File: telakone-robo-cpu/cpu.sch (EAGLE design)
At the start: 124 parts, among them K1 629105136821, X1 LIITTIMET_X3815-10, X2 MPT0.5/8-2.54, X3 MPT0.5/8-2.54, X4 MPT0.5/4-2.54, X5 MPT0.5/4-2.54, X7 MPT0.5/4-2.54

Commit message: inputs
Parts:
- removed R35: 5k90 1206, omat_ic_2:RES1206
- added C31, C35: 220u 16V D, EKE:CPOL-EUCT7343
- added C32: 10n, omat_ic_2:CAP0603
- added C33, C34: 2u2 50V 0805, omat_ic_2:CAP0805
- added C36, C37, C49: 100n, omat_ic_2:CAP0603
- added C38: 2u2, omat_ic_2:CAP0603
- added C39: 10n, cpu:CAP0603
- added C40, C41, C42, C43, C44, C45, C46, C48, C50, C51, C52, C56, C57, C59, C60: (no value), cpu:CAP0603
- added D6: LM75BD, omat_ic_2:LM75BD
- added D7: IIS328DQTR, omat_ic_2:IIS328DQTR
- added D8: MAX3430_SA, omat_ic_2:MAX3088_SA
- added D9: 74AHC14, cpu:74AHC14
- added L6: VLP8040-47U, omat_ic_2:VLP8040-47U
- added N2: TPS5430DDA, omat_ic_2:TPS5430DDA
- added Q1, Q2, Q3, Q4: PTC, cpu:PTC
- added R44, R45, R46, R47, R48, R53, R54, R55, R56, R57, R60, R61, R62, R63, R64, R65, R66, R67, R68, R69, R70, R71, R72, R73, R74, R75, R76, R77, R78, R79, R80, R81, R82, R83, R84: (no value), cpu:RES0603
- added R49: 10k0, omat_ic_2:RES0603
- added R50, R85: 5k90, omat_ic_2:RES0603
- added R51, R52, R59: 2k00, omat_ic_2:RES0603
- added R58: 121 1206, omat_ic_2:RES1206
- added V18: SK34A, omat_ic_2:SK34A
- added V19, V20, V21, V22: ESDAXXSC6, cpu:ESDAXXSC6
- added V36: SM712, omat_ic_2:SM712
- C28: value 2u2 -> 100n
- D11: value LM75BD -> 74AHC14; device omat_ic_2:LM75BD -> cpu:74AHC14
- D12: value IIS328DQTR -> 74AHC14; device omat_ic_2:IIS328DQTR -> cpu:74AHC14
- L1: value VLP8040-47U -> SDR1307-15UH; device omat_ic_2:VLP8040-47U -> cpu:INDSDR1307
- R2: value 5k90 -> 3k24
- R28: value 2k00 -> 2k2; device omat_ic_2:RES0603 -> cpu:RES0603
- R29: value 2k00 -> 5k90; device omat_ic_2:RES0603 -> cpu:RES0603
- V13: value SK34A -> SBRD10200; device omat_ic_2:SK34A -> cpu:SBRD10200
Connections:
- net LEDDATA1 renamed DIR1
- net LEDDATA2 renamed DIR3
- net LEDDATA3 renamed DIR5
- net N$3 renamed USBRENUM
- net SERVO10 renamed PULSE4
- net SERVO11 renamed DIR4
- net SERVO12 renamed PULSE5
- net SERVO4 renamed PULSE0
- net SERVO5 renamed DIR0
- net SERVO6 renamed PULSE1
- net SERVO7 renamed PULSE2
- net SERVO8 renamed DIR2
- net SERVO9 renamed PULSE3
- net SERVO_PWM_6 renamed PULSE_1
- removed net N$21: V24.C, V8.C, X3.1
- removed net SERVO_PWM_10: D5.A1
- removed net SERVO_PWM_11: D5.A2
- removed net SERVO_PWM_12: D5.A3
- removed net SERVO_PWM_4: D3.A1
- removed net SERVO_PWM_5: D3.A2
- removed net SERVO_PWM_7: D4.A1
- removed net SERVO_PWM_8: D4.A2
- removed net SERVO_PWM_9: D4.A3
- removed net USART2TX1: D3.A4
- removed net USART2TX2: D4.A4
- removed net USART2TX3: D5.A4
- new net ACCRTXHI: D8.A+, R58.2, V36.1
- new net ACCRTXLO: D8.B-, R58.1, V36.2
- new net DIR_0: D1G$3.PE8, D3.A2
- new net DIR_1: D1G$3.PE9, D3.A4
- new net DIR_2: D1G$3.PE10, D4.A2
- new net DIR_3: D1G$3.PE11, D4.A4
- new net DIR_4: D1G$3.PE12, D5.A2
- new net DIR_5: D1G$3.PE13, D5.A4
- new net ENABLE_N: D1G$3.PE14, D2.OE1, D2.OE2, D2.OE3, D2.OE4, D3.OE1, D3.OE2, D3.OE3, D3.OE4, D4.OE2, D4.OE3, D4.OE4, D5.OE1, D5.OE2, D5.OE3, D5.OE4, R44.1
- new net INPUT0: R29.2, V19.C
- new net INPUT1: R54.2, V19.C1
- new net INPUT10: R74.2, V21.C2
- new net INPUT11: R76.2, V21.C3
- new net INPUT12: R78.2, V22.C
- new net INPUT13: R80.2, V22.C1
- new net INPUT14: R82.2, V22.C2
- new net INPUT15: R84.2, V22.C3
- new net INPUT2: R56.2, V19.C2
- new net INPUT3: R60.2, V19.C3
- new net INPUT4: R62.2, V20.C
- new net INPUT5: R64.2, V20.C1
- new net INPUT6: R66.2, V20.C2
- new net INPUT7: R68.2, V20.C3
- new net INPUT8: R70.2, V21.C
- new net INPUT9: R72.2, V21.C1
- new net INPUT_0: D1G$2.PC8, D9G$1.Y
- new net INPUT_1: D1G$2.PC9, D9G$2.Y
- new net INPUT_10: D11G$5.Y, D1G$2.PD2
- new net INPUT_11: D11G$6.Y, D1G$2.PD3
- new net INPUT_12: D12G$1.Y, D1G$2.PD4
- new net INPUT_13: D12G$2.Y, D1G$2.PD5
- new net INPUT_14: D12G$3.Y, D1G$2.PD6
- new net INPUT_15: D12G$4.Y, D1G$2.PD7
- new net INPUT_2: D1G$2.PC10, D9G$3.Y
- new net INPUT_3: D1G$2.PC11, D9G$4.Y
- new net INPUT_4: D1G$2.PC12, D9G$5.Y
- new net INPUT_5: D1G$2.PC13, D9G$6.Y
- new net INPUT_6: D11G$1.Y, D1G$1.PC14/OSC32IN
- new net INPUT_7: D11G$2.Y, D1G$1.PC15/OSC32OUT
- new net INPUT_8: D11G$3.Y, D1G$2.PD0
- new net INPUT_9: D11G$4.Y, D1G$2.PD1
- new net N$38: C39.1, D9G$1.A, R28.2, R29.1
- new net N$41: C40.1, D9G$2.A, R53.2, R54.1
- new net N$43: C41.1, D9G$3.A, R55.2, R56.1
- new net N$45: C42.1, D9G$4.A, R57.2, R60.1
- new net N$47: C43.1, D9G$5.A, R61.2, R62.1
- new net N$49: C44.1, D9G$6.A, R63.2, R64.1
- new net N$51: C45.1, D11G$1.A, R65.2, R66.1
- new net N$53: C46.1, D11G$2.A, R67.2, R68.1
- new net N$55: C48.1, D11G$3.A, R69.2, R70.1
- new net N$57: C50.1, D11G$4.A, R71.2, R72.1
- new net N$59: C51.1, D11G$5.A, R73.2, R74.1
- new net N$61: C52.1, D11G$6.A, R75.2, R76.1
- new net N$63: C56.1, D12G$1.A, R77.2, R78.1
- new net N$65: C57.1, D12G$2.A, R79.2, R80.1
- new net N$67: C59.1, D12G$3.A, R81.2, R82.1
- new net N$69: C60.1, D12G$4.A, R83.2, R84.1
- new net OUT1X: Q1.1, V24.C, V8.C
- new net OUT2X: Q2.1, V10.C, V24.C1
- new net OUT3X: Q3.1, V11.C, V24.C2
- new net OUT4X: Q4.1, V12.C, V24.C3
- new net OUT_1: D1G$2.PC0, R11.1, V3.G
- new net OUT_2: D1G$2.PC1, R13.1, V5.G
- new net OUT_3: R14.1, V7.G
- new net OUT_4: R15.1, V9.G
- new net PULSE_0: D1G$2.PD12, D3.A1
- new net PULSE_2: D1G$2.PC6, D4.A1
- new net PULSE_3: D1G$3.PE5, D4.A3
- new net PULSE_4: D1G$2.PB8, D5.A1
- new net PULSE_5: D1G$2.PB9, D5.A3
- new net SPI1MISO: D1G$1.PB4/TRSTL
- new net SPI1MOSI: D1G$2.PB5
- new net SPI1SCK: D1G$1.PB3/TDO
- new net SPI_CS_PS2_N: D1G$2.PA8
- new net USART1RX: D1G$2.PA10, D8.RO
- new net USART1TX: D1G$2.PA9, D8.DI
- new net USART1TXE: D1G$2.PD15, D8.DE, D8.RE~, R59.2
- net +12V: now also C33.1, C34.1, N2.VIN, R85.1; no longer R35.1
- net +3V3: now also C31.+, C36.1, C37.1, C38.1, C49.1, D11G$1.VCC, D12G$1.VCC, D6.VCC, D7.CS, D7.RSVD1, D7.VDD, D7.VDDIO, D8.VCC, D9G$1.VCC, L6.B, R44.2, R49.1, R51.2, R52.2; no longer C1.+, D11.VCC, D12.CS, D12.RSVD1, D12.VDD, D12.VDDIO, L1.B, R1.1, R28.2, R29.2
- net +5V: now also C1.+, C35.+, L1.2, R1.1
- net GND: now also C31.-, C33.2, C34.2, C35.-, C36.2, C37.2, C38.2, C39.2, C40.2, C41.2, C42.2, C43.2, C44.2, C45.2, C46.2, C48.2, C49.2, C50.2, C51.2, C52.2, C56.2, C57.2, C59.2, C60.2, D11G$1.GND, D12G$1.GND, D6.A0, D6.A1, D6.A2, D6.GND, D7.EP, D7.GND@1, D7.GND@2, D7.GND@3, D7.GND@4, D7.RSVD2, D7.SAO/SPISDO, D8.GND, D9G$1.GND, N2.EP, N2.GND, R28.1, R45.1, R46.1, R47.1, R48.1, R50.2, R53.1, R55.1, R57.1, R59.1, R61.1, R63.1, R65.1, R67.1, R69.1, R71.1, R73.1, R75.1, R77.1, R79.1, R81.1, R83.1, V18.A, V19.A, V19.A1, V20.A, V20.A1, V21.A, V21.A1, V22.A, V22.A1, V36.3; no longer D11.A0, D11.A1, D11.A2, D11.GND, D12.EP, D12.GND@1, D12.GND@2, D12.GND@3, D12.GND@4, D12.RSVD2, D12.SAO/SPISDO, D2.OE1, D2.OE2, D2.OE3, D2.OE4, D3.OE1, D3.OE2, D3.OE3, D3.OE4, D4.OE2, D4.OE3, D4.OE4, D5.OE1, D5.OE2, D5.OE3, D5.OE4
- net I2C1SCL: now also D6.SCL, D7.SCL/SPICLK, R52.1; no longer D11.SCL, D12.SCL/SPICLK, R29.1
- net I2C1SDA: now also D6.SDA, D7.SDA/SPISDI, R51.1; no longer D11.SDA, D12.SDA/SPISDI, R28.1
- net LEDDATA: now also R48.2
- net MEAS12V: now also R85.2; no longer R35.2
- net N$1: now also L1.1; no longer L1.A
- net N$17: now also C32.1, L6.A, N2.PH, V18.C; no longer V12.C, V24.C3, X3.7
- net N$19: now also C32.2, N2.BOOT; no longer V11.C, V24.C2, X3.5
- net N$20: now also N2.SENSE, R49.2, R50.1; no longer V10.C, V24.C1, X3.3
- net OUT1: now also Q1.2, X3.1; no longer D1G$2.PC0, R11.1, V3.G
- net OUT2: now also Q2.2, X3.3; no longer D1G$2.PC1, R13.1, V5.G
- net OUT3: now also Q3.2, X3.5; no longer R14.1, V7.G
- net OUT4: now also Q4.2, X3.7; no longer R15.1, V9.G
- net SERVO1: now also R45.2
- net SERVO2: now also R46.2
- net SERVO3: now also R47.2
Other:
- note added: "+3.3V 1A"
- note added: "+5V 3A"
- note added: "VMAX 19 V VTH+ 8.1 V VTH- 3.3 V"
- note removed: "I2C1"

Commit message: input liittimet, ena outputit
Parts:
- added C61: 100n, omat_ic_2:CAP0603
- added C62: 2u2, omat_ic_2:CAP0603
- added C63, C64: (no value), cpu:CAP0603
- added C65: (no value), cpu:CAP0805
- added D13, D14: 74AHCT125, cpu:74AHCT125
- added L7: IND0603, omat_ic_2:IND0603
- added L8: IND0603, cpu:IND0603
- added R35, R86, R87, R88, R89, R90, R91, R92, R93, R94, R95, R96: (no value), cpu:RES0603
- added V23, V25: ESDAXXSC6, cpu:ESDAXXSC6
- added X10, X9: MPT0.5/8-2.54, cpu:MPT0.5/8-2.54
- added X11, X12, X13, X14: MPT0.5/4-2.54, cpu:MPT0.5/4-2.54
- added X8: PS-JOYSTICK, cpu:PS-JOYSTICK
- added Y1, Y2, Y3, Y4: PTH2.6-5.5SQ, EKE:PTH2.6-5.5SQ
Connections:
- removed net SPI1SCK: D1G$1.PB3/TDO
- new net ENA0: R89.2, V23.C, X11.1
- new net ENA1: R90.2, V23.C1, X11.2
- new net ENA2: R91.2, V23.C2, X11.3
- new net ENA3: R92.2, V23.C3, X11.4
- new net ENA4: R93.2, V25.C, X12.1
- new net ENA5: R94.2, V25.C1, X12.2
- new net ENA_0: D13.A1, D1G$3.PG0
- new net ENA_1: D13.A2, D1G$3.PG1
- new net ENA_2: D13.A3, D1G$3.PG2
- new net ENA_3: D13.A4, D1G$3.PG3
- new net ENA_4: D14.A1, D1G$3.PG4
- new net ENA_5: D14.A2, D1G$3.PG5
- new net I2CVCC: C65.1, L8.1, X14.1
- new net N$21: R86.1, X8.CMD
- new net N$3: R35.1, X8.DATA
- new net N$39: R87.1, X8.ATT
- new net N$42: R88.1, X8.CLK
- new net N$44: D13.Y1, R89.1
- new net N$46: D13.Y2, R90.1
- new net N$48: D13.Y3, R91.1
- new net N$50: D13.Y4, R92.1
- new net N$52: D14.Y1, R93.1
- new net N$54: D14.Y2, R94.1
- new net N$56: D14.Y3, R95.1
- new net N$58: D14.Y4, R96.1
- new net N$60: X14.2
- new net N$62: X14.4
- new net PSVCC: C61.1, C62.1, L7.1, X8.VCC
- new net SPARE1: R95.2, V25.C2, X12.3
- new net SPARE2: R96.2, V25.C3, X12.4
- new net SPARE_1: D14.A3, D1G$3.PG6
- new net SPARE_2: D14.A4, D1G$3.PG7
- new net SPI1CLK: D1G$1.PB3/TDO, R88.2
- net +12V: now also X13.1, X13.2, X13.3, X13.4
- net +3V3: now also L7.2
- net +5V: now also C63.1, C64.1, D13.VCC, D14.VCC, L8.2
- net ENABLE_N: now also D13.OE1, D13.OE2, D13.OE3, D13.OE4, D14.OE2, D14.OE3, D14.OE4
- net GND: now also C61.2, C62.2, C63.2, C64.2, C65.2, D13.GND, D14.GND, V23.A, V23.A1, V25.A, V25.A1, X14.3, X8.GND, Y1.1, Y2.1, Y3.1, Y4.1
- net INPUT0: now also X9.1
- net INPUT1: now also X9.2
- net INPUT10: now also X10.3
- net INPUT11: now also X10.4
- net INPUT12: now also X10.5
- net INPUT13: now also X10.6
- net INPUT14: now also X10.7
- net INPUT15: now also X10.8
- net INPUT2: now also X9.3
- net INPUT3: now also X9.4
- net INPUT4: now also X9.5
- net INPUT5: now also X9.6
- net INPUT6: now also X9.7
- net INPUT7: now also X9.8
- net INPUT8: now also X10.1
- net INPUT9: now also X10.2
- net SPI1MISO: now also R35.2
- net SPI1MOSI: now also R86.2
- net SPI_CS_PS2_N: now also R87.2
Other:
- note added: "MOUNTING HOLES"
- moved on the sheet: C25, C29, C30, C36, C37, C38, C49, D1G$2, D1G$3, D3, D4, D5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

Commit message: i2c expander yms
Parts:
- added C66, C67: (no value), cpu:CAP0805
- added D15: PCA9517, cpu:PCA9517
- added L9: IND0603, cpu:IND0603
- added R100, R99: 2k00, omat_ic_2:RES0603
- added X15: MPT0.5/4-2.54, cpu:MPT0.5/4-2.54
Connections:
- removed net N$60: X14.2
- removed net N$62: X14.4
- new net I2CSCL: D15.SCLB, R100.1, X14.4
- new net I2CSDA: D15.SDAB, R99.1, X14.2
- net +3V3: now also C67.1, D15.VCCA, L8.2
- net +5V: now also L9.1; no longer L8.2
- net ACCRTXHI: now also X15.3
- net ACCRTXLO: now also X15.4
- net GND: now also C66.2, C67.2, D12G$5.A, D12G$6.A, D15.GND
- net I2C1SCL: now also D15.SCLA
- net I2C1SDA: now also D15.SDAA
- net I2CVCC: now also C66.1, D15.EN, D15.VCCB, L9.2, R100.2, R99.2
- net OUT_3: now also D1G$2.PB10
- net OUT_4: now also D1G$2.PB11
- net SERVO_PWM_3: now also D1G$2.PB0
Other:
- note removed: "TODO SERVO_PWM_3 NOT CONNECTED"
- moved on the sheet: C49, C65, D8, L8, R58, R59, V36

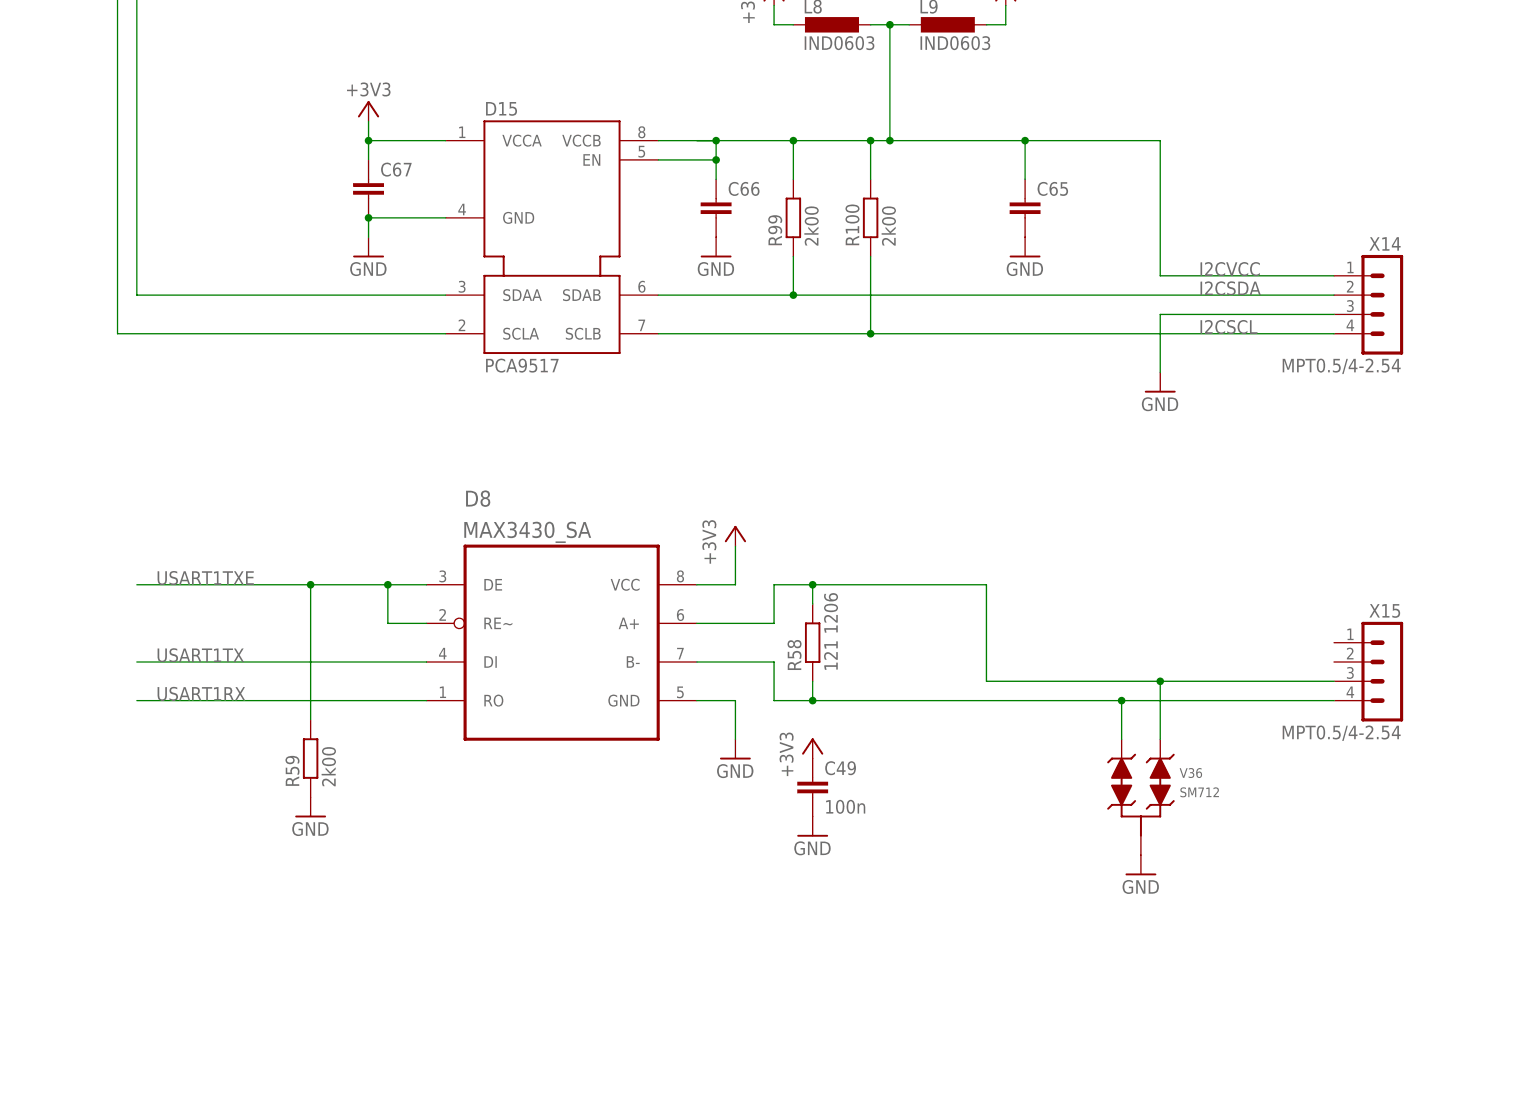
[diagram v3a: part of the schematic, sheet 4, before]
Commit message: finish schematics, rough initial placement
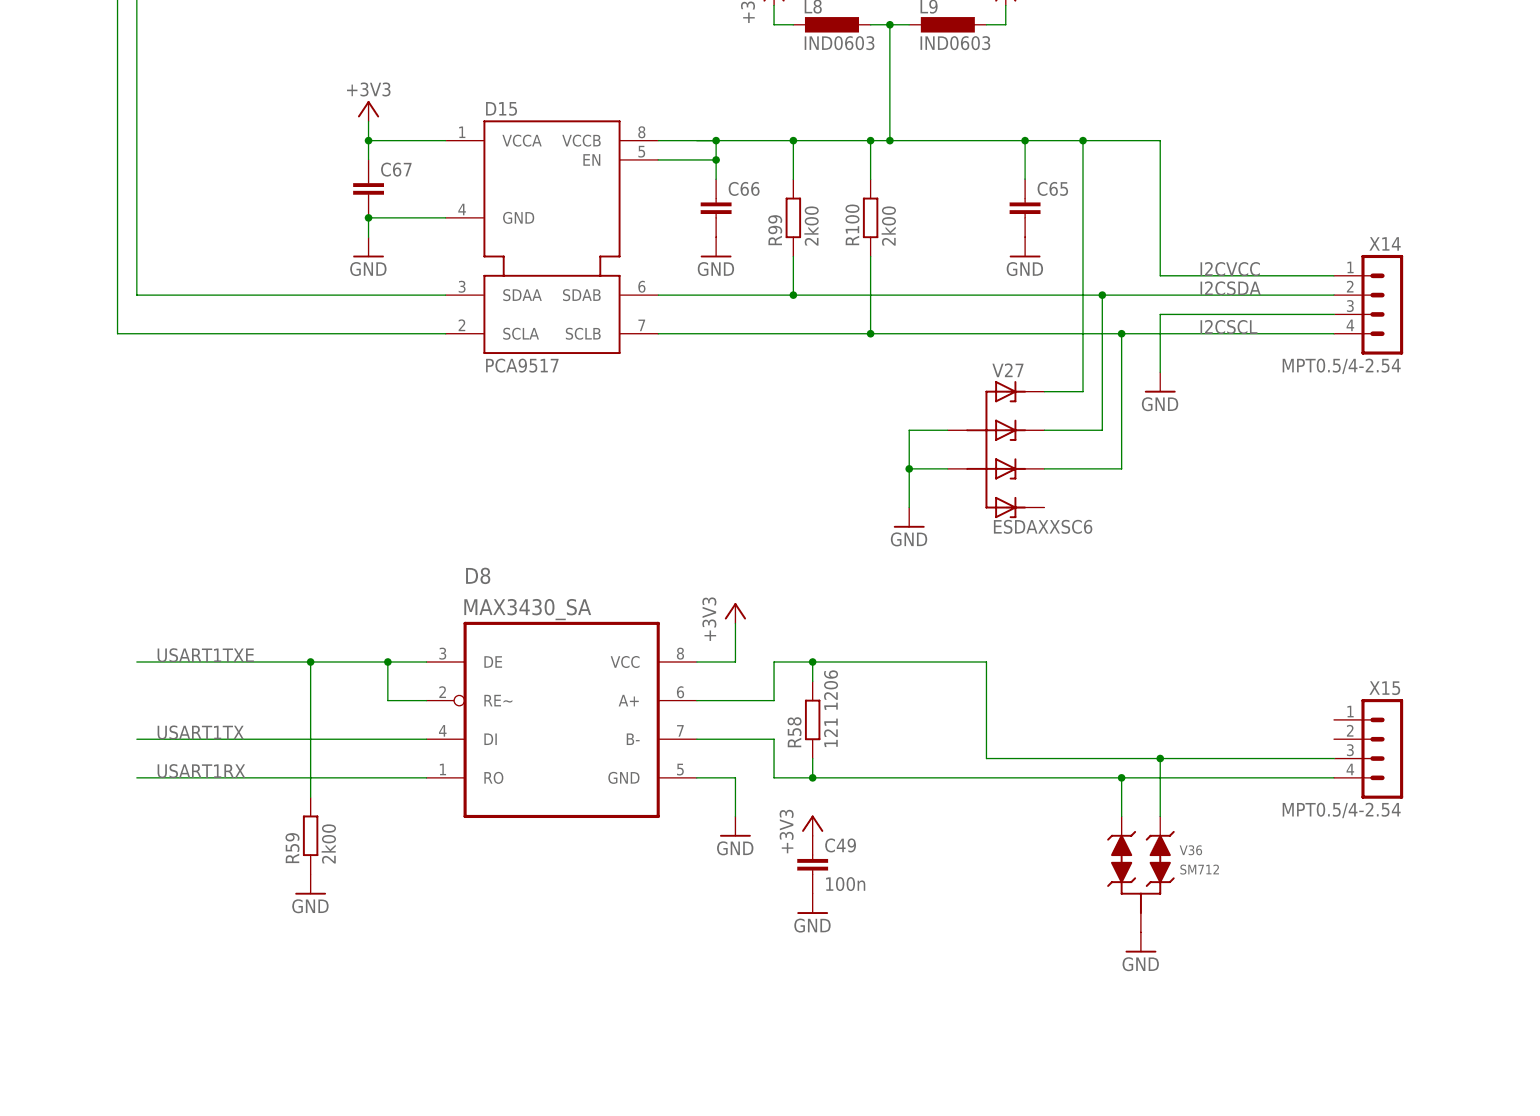
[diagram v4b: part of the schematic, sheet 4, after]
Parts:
- added C68, C69: (no value), cpu:CAP0805
- added V26: SRV05-4, cpu:SRV05-4
- added V27: ESDAXXSC6, cpu:ESDAXXSC6
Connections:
- new net SERVO_VCC1: C68.1
- new net SERVO_VCC2: C69.1
- net GND: now also C68.2, C69.2, V26.GND, V27.A, V27.A1
- net I2CSCL: now also V27.C2
- net I2CSDA: now also V27.C1
- net I2CVCC: now also V27.C
- net USB_DM: now also V26.D
- net USB_DP: now also V26.C
- net VUSB: now also V26.VCC
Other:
- moved on the sheet: C49, C6, C7, D8, L4, L5, R58, R59, V36, X15

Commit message: signals routed, almost
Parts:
- added X16: MPT0.5/4-2.54, cpu:MPT0.5/4-2.54
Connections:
- removed net SERVO_VCC1: C68.1
- removed net SERVO_VCC2: C69.1
- new net ENABLE_PWM_N: D1G$3.PG9, D2.OE1, D2.OE2, D2.OE3, D2.OE4
- net ACCRTXHI: now also V36.2; no longer V36.1
- net ACCRTXLO: now also V36.1; no longer V36.2
- net DIR0: now also V14.C2; no longer V14.C1
- net DIR1: now also V14.C; no longer V14.C3
- net DIR2: now also V15.C2; no longer V15.C1
- net DIR3: now also V15.C; no longer V15.C3
- net DIR4: now also V17.C2; no longer V17.C1
- net DIR5: now also V17.C; no longer V17.C3
- net ENA0: now also V23.C3; no longer V23.C
- net ENA1: now also V23.C2; no longer V23.C1
- net ENA2: now also V23.C1; no longer V23.C2
- net ENA3: now also V23.C; no longer V23.C3
- net ENA4: now also V25.C3; no longer V25.C
- net ENA5: now also V25.C2; no longer V25.C1
- net ENABLE_N: now also D14.OE1, D4.OE1; no longer D2.OE1, D2.OE2, D2.OE3, D2.OE4
- net GND: now also X16.1, X16.4, X2.3, X2.6; no longer X2.5, X2.8
- net I2CSCL: now also V27.C1; no longer V27.C2
- net I2CSDA: now also V27.C2; no longer V27.C1
- net I2CVCC: now also V27.C3; no longer V27.C
- net INPUT0: now also V19.C1; no longer V19.C
- net INPUT1: now also V19.C; no longer V19.C1
- net INPUT10: now also V21.C3; no longer V21.C2
- net INPUT11: now also V21.C2; no longer V21.C3
- net INPUT12: now also V22.C1; no longer V22.C
- net INPUT13: now also V22.C; no longer V22.C1
- net INPUT14: now also V22.C3; no longer V22.C2
- net INPUT15: now also V22.C2; no longer V22.C3
- net INPUT2: now also V19.C3; no longer V19.C2
- net INPUT3: now also V19.C2; no longer V19.C3
- net INPUT4: now also V20.C1; no longer V20.C
- net INPUT5: now also V20.C; no longer V20.C1
- net INPUT6: now also V20.C3; no longer V20.C2
- net INPUT7: now also V20.C2; no longer V20.C3
- net INPUT8: now also V21.C1; no longer V21.C
- net INPUT9: now also V21.C; no longer V21.C1
- net LEDDATA: now also V6.C, X16.3; no longer V6.C3, X2.7
- net LED_VCC: now also C69.1, X16.2; no longer X2.6
- net PULSE0: now also V14.C3; no longer V14.C
- net PULSE1: now also V14.C1; no longer V14.C2
- net PULSE2: now also V15.C3; no longer V15.C
- net PULSE3: now also V15.C1; no longer V15.C2
- net PULSE4: now also V17.C3; no longer V17.C
- net PULSE5: now also V17.C1; no longer V17.C2
- net SERVO1: now also V6.C3; no longer V6.C
- net SERVO2: now also V6.C2, X2.5; no longer V6.C1, X2.3
- net SERVO3: now also V6.C1, X2.8; no longer V6.C2, X2.4
- net SERVO_VCC: now also C68.1, X2.4, X2.7
- net SPARE1: now also V25.C1; no longer V25.C2
- net SPARE2: now also V25.C; no longer V25.C3
- net SPI_CS_PS2_N: now also D1G$2.PA1; no longer D1G$2.PA8
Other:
- moved on the sheet: R45, R46, R47, R48, V27, V6, X2
